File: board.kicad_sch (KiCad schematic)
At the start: 6 parts, among them U1 MC68060RC50, U2 XC95144XL-5TQG100C, U3 SST39VF1601C-70-4C-EKE, U4 IS61WV51216BLL-10TLI, U5 IS61WV51216BLL-10TLI, U6 SST39VF1601C-70-4C-EKE

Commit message: First version
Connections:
- net at U2.11 (IO): no longer U1.T14 (*TA)
- net at U2.12 (IO): no longer U1.R16 (*TS)
- net at U2.13 (IO): no longer U1.Q14 (*SAS)
- net at U2.14 (IO): no longer U1.R15 (*TIP)
- net at U2.15 (IO): no longer U1.N16 (R/*W)
- net at U2.20 (IO): no longer U1.K15 (*CLA)
- net at U2.24 (IO): no longer U1.P17 (SIZ0)
- net at U2.25 (IO): no longer U1.P16 (SIZ1)
- net at U2.28 (IO): no longer U1.Q8 (*CLKEN)
- net at U2.30 (IO): no longer U1.P2 (TT1)
- net at U2.32 (IO): no longer U1.P3 (TT0)
- net at U2.33 (IO): no longer U1.T8 (*IPL0)
- net at U2.34 (IO): no longer U1.T7 (*IPL1)
- net at U2.35 (IO): no longer U1.T6 (*IPL2)
- net at U2.36 (IO): no longer U1.S1 (*IPEND)
- net at U2.37 (IO): no longer U1.T11 (*AVEC)
- net at U2.39 (IO): no longer U1.Q13 (PST4)
- net at U2.40 (IO): no longer U1.T16 (PST3)
- net at U2.41 (IO): no longer U1.R14 (PST2)
- net at U2.42 (IO): no longer U1.S14 (PST1)
- net at U2.43 (IO): no longer U1.T15 (PST0)
- net at U2.45 (TDI): no longer U1.S3 (TDI)
- net at U2.46 (IO): no longer U1.S6 (*MDIS)
- net at U2.47 (IO): no longer U1.S5 (TMS)
- net at U2.48 (IO): no longer U1.S4 (TCK)
- net at U2.49 (IO): no longer U1.R3 (*RSTO)
- net at U2.50 (IO): no longer U1.S7 (*RSTI)
- net at U2.52 (IO): no longer U1.K17 (TM2)
- net at U2.53 (IO): no longer U1.M18 (TM1)
- net at U2.54 (IO): no longer U1.N18 (TM0)
- net at U2.55 (IO): no longer U1.Q1 (UPA1)
- net at U2.56 (IO): no longer U1.Q3 (UPA0)
- net U1B-UPA0: now reaches U2.81 (NC)

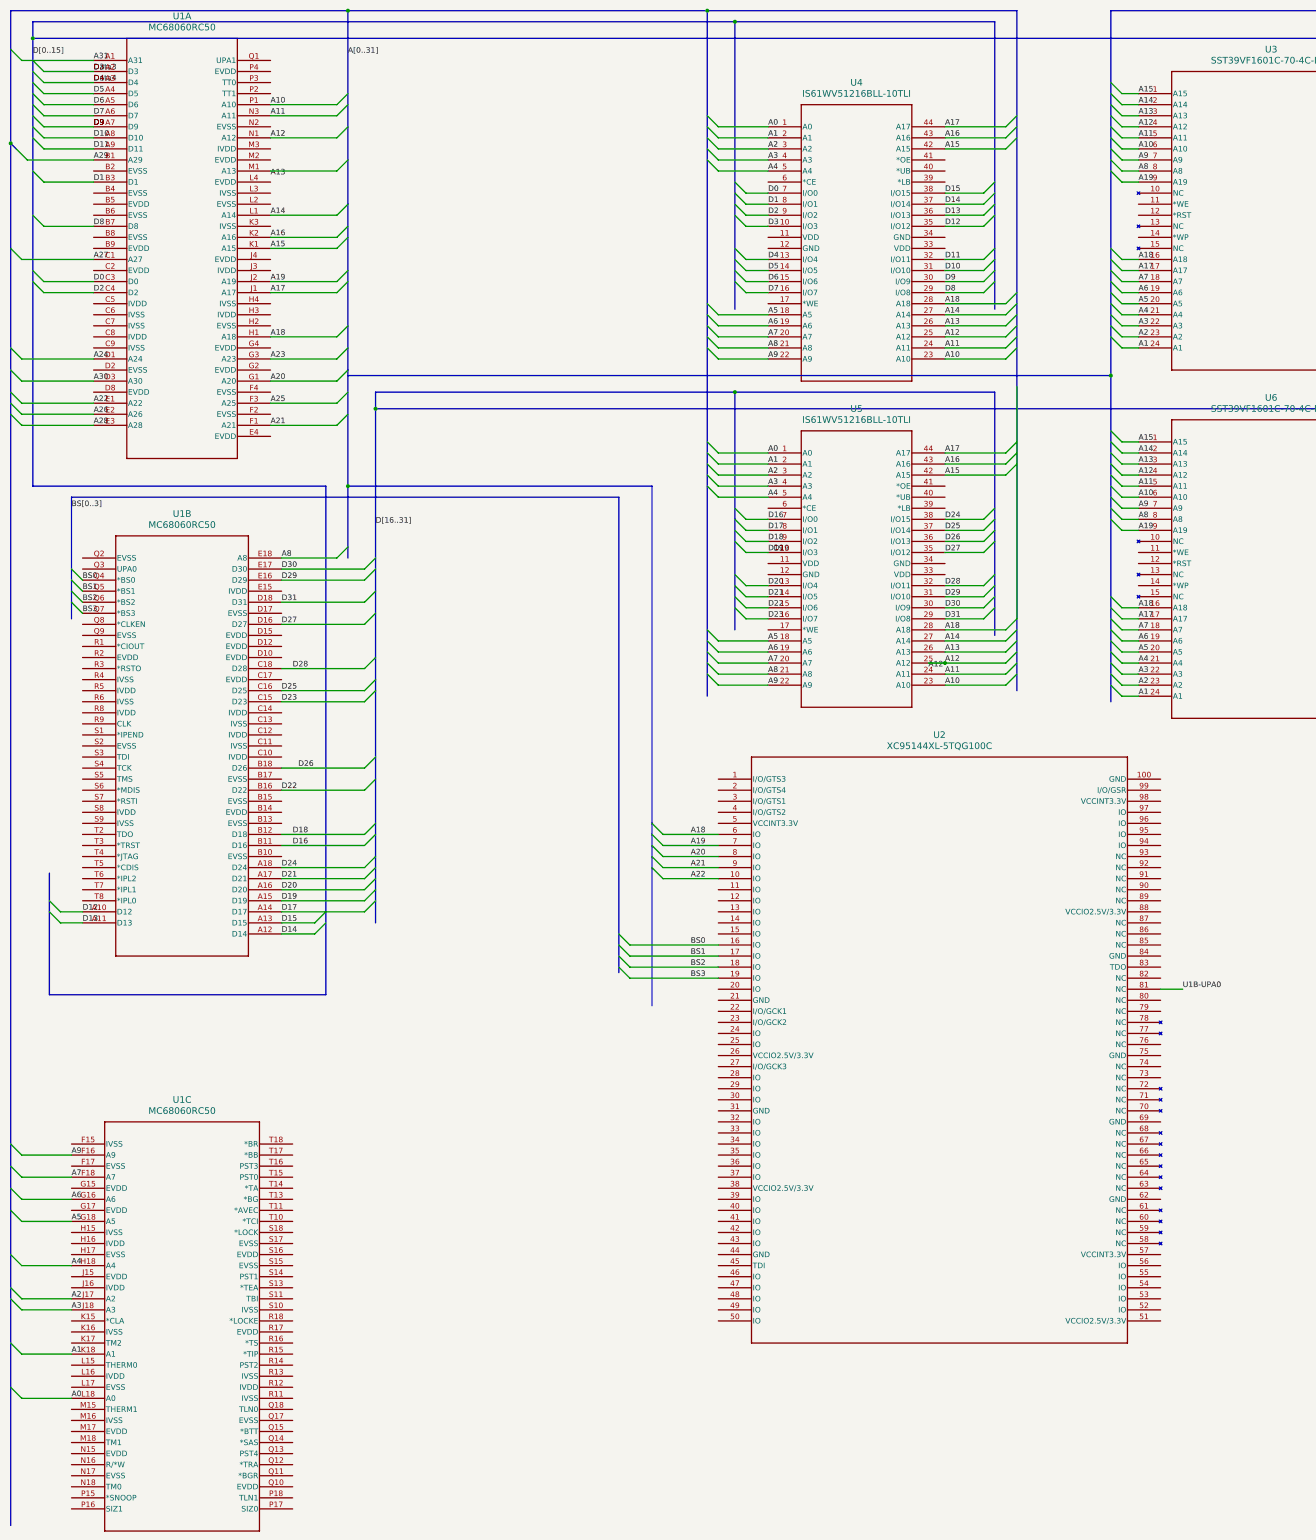
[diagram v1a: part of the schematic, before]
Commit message: Power planes added
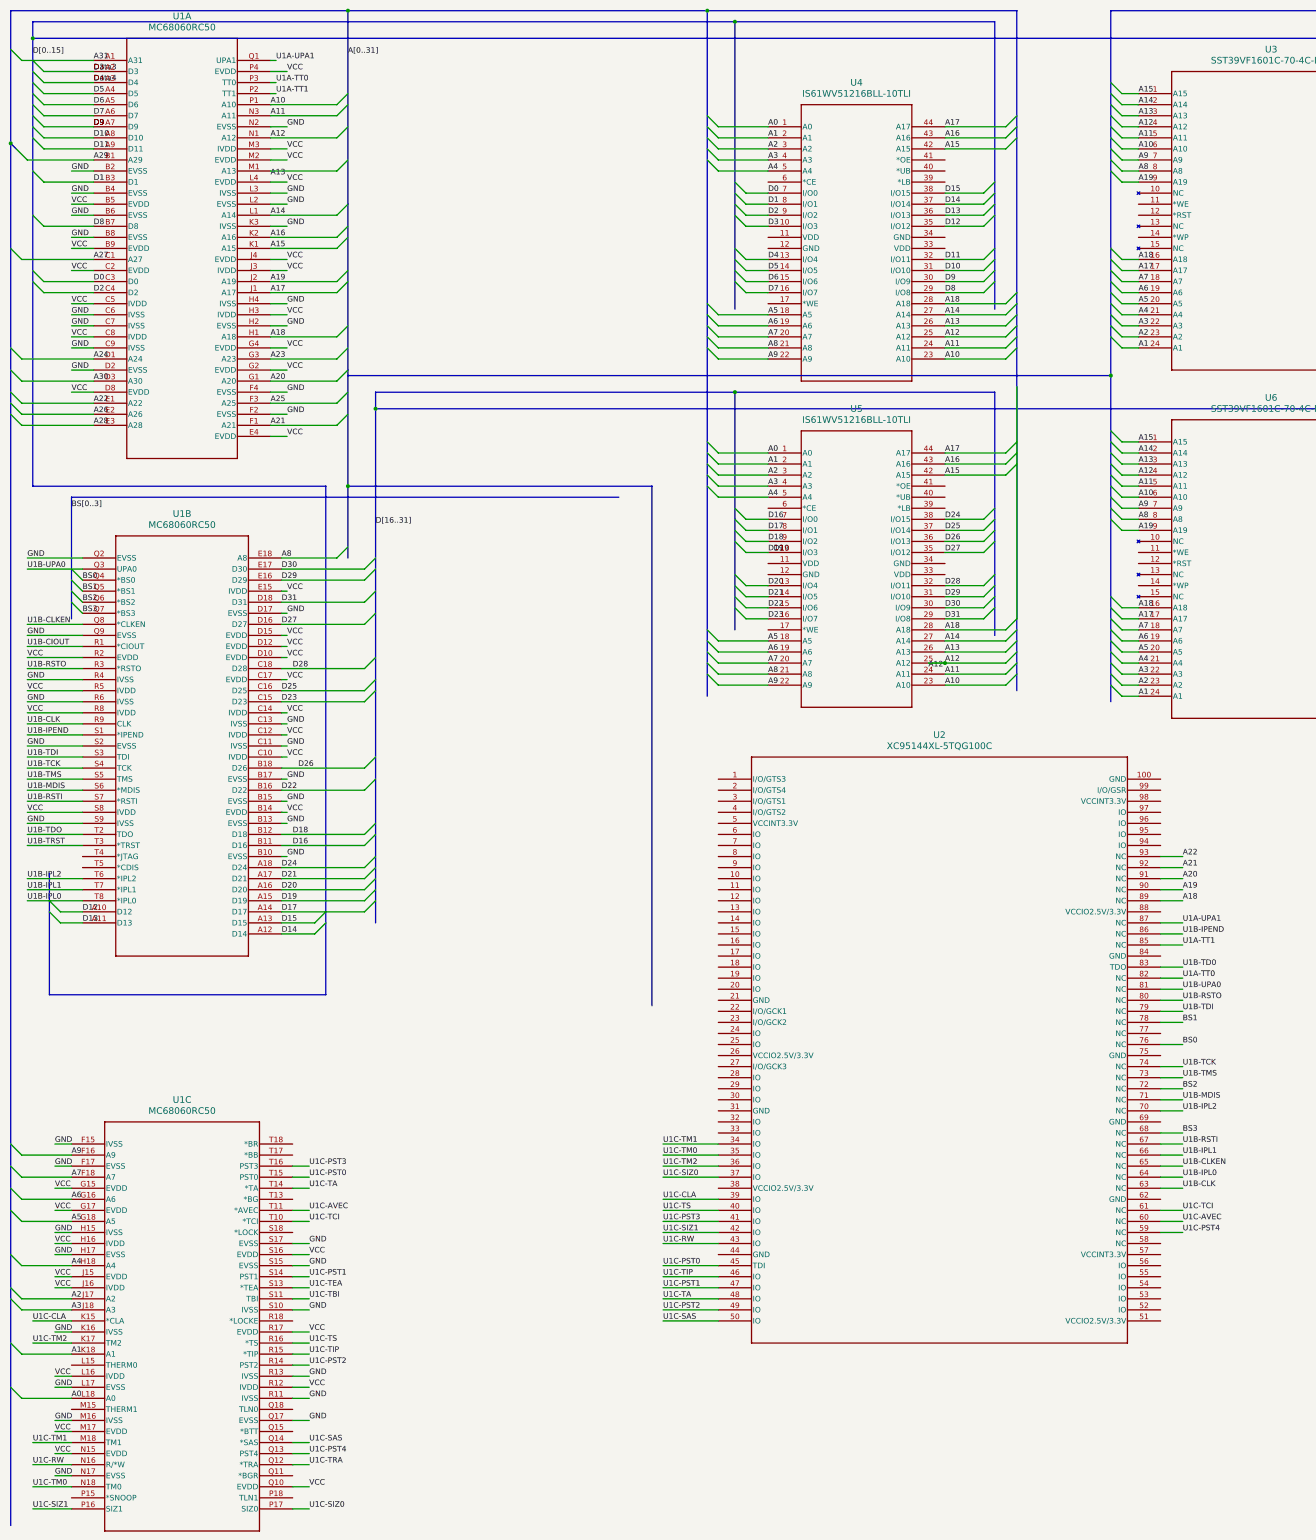
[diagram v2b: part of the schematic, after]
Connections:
- net A18: now also U2.89 (NC); no longer U2.6 (IO)
- net A19: now also U2.90 (NC); no longer U2.7 (IO)
- net A20: now also U2.91 (NC); no longer U2.8 (IO)
- net A21: now also U2.92 (NC); no longer U2.9 (IO)
- net A22: now also U2.93 (NC); no longer U2.10 (IO)
- net BS0: now also U2.76 (NC); no longer U2.16 (IO)
- net BS1: now also U2.78 (NC); no longer U2.17 (IO)
- net BS2: now also U2.72 (NC); no longer U2.18 (IO)
- net BS3: now also U2.68 (NC); no longer U2.19 (IO)
- net U1B-UPA0: now also U1.Q3 (UPA0)
- net U1C-TM1: now reaches U2.34 (IO)
- net U1C-TM1: now also U1.M18 (TM1)
- net U1C-TM0: now reaches U2.35 (IO)
- net U1C-TM0: now also U1.N18 (TM0)
- net U1C-TM2: now reaches U2.36 (IO)
- net U1C-TM2: now also U1.K17 (TM2)
- net U1C-SIZ0: now reaches U2.37 (IO)
- net U1C-SIZ0: now also U1.P17 (SIZ0)
- net U1C-CLA: now reaches U2.39 (IO)
- net U1C-CLA: now also U1.K15 (*CLA)
- net U1C-TS: now reaches U2.40 (IO)
- net U1C-TS: now also U1.R16 (*TS)
- net U1C-PST3: now reaches U2.41 (IO)
- net U1C-PST3: now also U1.T16 (PST3)
- net U1C-SIZ1: now reaches U2.42 (IO)
- net U1C-SIZ1: now also U1.P16 (SIZ1)
- net U1C-RW: now reaches U2.43 (IO)
- net U1C-RW: now also U1.N16 (R/*W)
- net U1C-PST0: now reaches U2.45 (TDI)
- net U1C-PST0: now also U1.T15 (PST0)
- net U1C-TIP: now reaches U2.46 (IO)
- net U1C-TIP: now also U1.R15 (*TIP)
- net U1C-PST1: now reaches U2.47 (IO)
- net U1C-PST1: now also U1.S14 (PST1)
- net U1C-TA: now reaches U2.48 (IO)
- net U1C-TA: now also U1.T14 (*TA)
- net U1C-PST2: now reaches U2.49 (IO)
- net U1C-PST2: now also U1.R14 (PST2)
- net U1C-SAS: now reaches U2.50 (IO)
- net U1C-SAS: now also U1.Q14 (*SAS)
- net U1C-PST4: now reaches U2.59 (NC)
- net U1C-PST4: now also U1.Q13 (PST4)
- net U1C-AVEC: now reaches U2.60 (NC)
- net U1C-AVEC: now also U1.T11 (*AVEC)
- net U1C-TCI: now reaches U2.61 (NC)
- net U1C-TCI: now also U1.T10 (*TCI)
- net U1B-CLK: now reaches U2.63 (NC)
- net U1B-CLK: now also U1.R9 (CLK)
- net U1B-IPL0: now reaches U2.64 (NC)
- net U1B-IPL0: now also U1.T8 (*IPL0)
- net U1B-CLKEN: now reaches U2.65 (NC)
- net U1B-CLKEN: now also U1.Q8 (*CLKEN)
- net U1B-IPL1: now reaches U2.66 (NC)
- net U1B-IPL1: now also U1.T7 (*IPL1)
- net U1B-RSTI: now reaches U2.67 (NC)
- net U1B-RSTI: now also U1.S7 (*RSTI)
- net U1B-IPL2: now reaches U2.70 (NC)
- net U1B-IPL2: now also U1.T6 (*IPL2)
- net U1B-MDIS: now reaches U2.71 (NC)
- net U1B-MDIS: now also U1.S6 (*MDIS)
- net U1B-TMS: now reaches U2.73 (NC)
- net U1B-TMS: now also U1.S5 (TMS)
- net U1B-TCK: now reaches U2.74 (NC)
- net U1B-TCK: now also U1.S4 (TCK)
- net U1B-TDI: now reaches U2.79 (NC)
- net U1B-TDI: now also U1.S3 (TDI)
- net U1B-RSTO: now reaches U2.80 (NC)
- net U1B-RSTO: now also U1.R3 (*RSTO)
- net U1A-TT0: now reaches U2.82 (NC)
- net U1A-TT0: now also U1.P3 (TT0)
- net U1B-TD0: now reaches U2.83 (TDO)
- net U1A-TT1: now reaches U2.85 (NC)
- net U1A-TT1: now also U1.P2 (TT1)
- net U1B-IPEND: now reaches U2.86 (NC)
- net U1B-IPEND: now also U1.S1 (*IPEND)
- net U1A-UPA1: now reaches U2.87 (NC)
- net U1A-UPA1: now also U1.Q1 (UPA1)
- net GND: now reaches U1.B2 (EVSS)
- net GND: now also U1.B10 (EVSS), U1.B13 (EVSS), U1.B15 (EVSS), U1.B17 (EVSS), U1.B4 (EVSS), U1.B6 (EVSS), U1.B8 (EVSS), U1.C11 (IVSS), U1.C13 (IVSS), U1.C6 (IVSS), U1.C7 (IVSS), U1.C9 (IVSS), U1.D17 (EVSS), U1.D2 (EVSS), U1.F15 (IVSS), U1.F17 (EVSS), U1.F2 (EVSS), U1.F4 (EVSS), U1.H15 (IVSS), U1.H17 (EVSS), U1.H2 (EVSS), U1.H4 (IVSS), U1.K16 (IVSS), U1.K3 (IVSS), U1.L17 (EVSS), U1.L2 (EVSS), U1.L3 (IVSS), U1.M16 (IVSS), U1.N17 (EVSS), U1.N2 (EVSS), U1.Q17 (EVSS), U1.Q2 (EVSS), U1.Q9 (EVSS), U1.R11 (IVSS), U1.R13 (IVSS), U1.R4 (IVSS), U1.R6 (IVSS), U1.S10 (IVSS), U1.S15 (EVSS), U1.S17 (EVSS), U1.S2 (EVSS), U1.S9 (IVSS)
- net VCC: now reaches U1.B5 (EVDD)
- net VCC: now also U1.B14 (EVDD), U1.B9 (EVDD), U1.C10 (IVDD), U1.C12 (IVDD), U1.C14 (IVDD), U1.C17 (EVDD), U1.C2 (EVDD), U1.C5 (IVDD), U1.C8 (IVDD), U1.D10 (EVDD), U1.D12 (EVDD), U1.D15 (EVDD), U1.D8 (EVDD), U1.E15 (IVDD), U1.E4 (EVDD), U1.G15 (EVDD), U1.G17 (EVDD), U1.G2 (EVDD), U1.G4 (EVDD), U1.H16 (IVDD), U1.H3 (IVDD), U1.J15 (EVDD), U1.J16 (IVDD), U1.J3 (IVDD), U1.J4 (EVDD), U1.L16 (IVDD), U1.L4 (EVDD), U1.M17 (EVDD), U1.M2 (EVDD), U1.M3 (IVDD), U1.N15 (EVDD), U1.P4 (EVDD), U1.Q10 (EVDD), U1.R12 (IVDD), U1.R17 (EVDD), U1.R2 (EVDD), U1.R5 (IVDD), U1.R8 (IVDD), U1.S16 (EVDD), U1.S8 (IVDD)
- net U1C-TRA: now reaches U1.Q12 (*TRA)
- net U1C-TBI: now reaches U1.S11 (TBI)
- net U1C-TEA: now reaches U1.S13 (*TEA)
- net U1B-CIOUT: now reaches U1.R1 (*CIOUT)
- net U1B-TDO: now reaches U1.T2 (TDO)
- net U1B-TRST: now reaches U1.T3 (*TRST)
